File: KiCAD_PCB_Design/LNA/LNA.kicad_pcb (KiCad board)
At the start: 2 copper layers, 47 x 33 mm, 12 parts, among them P1 SMA, P2 3V_SUPPLY, P3 SMA, U1 MGA-62563

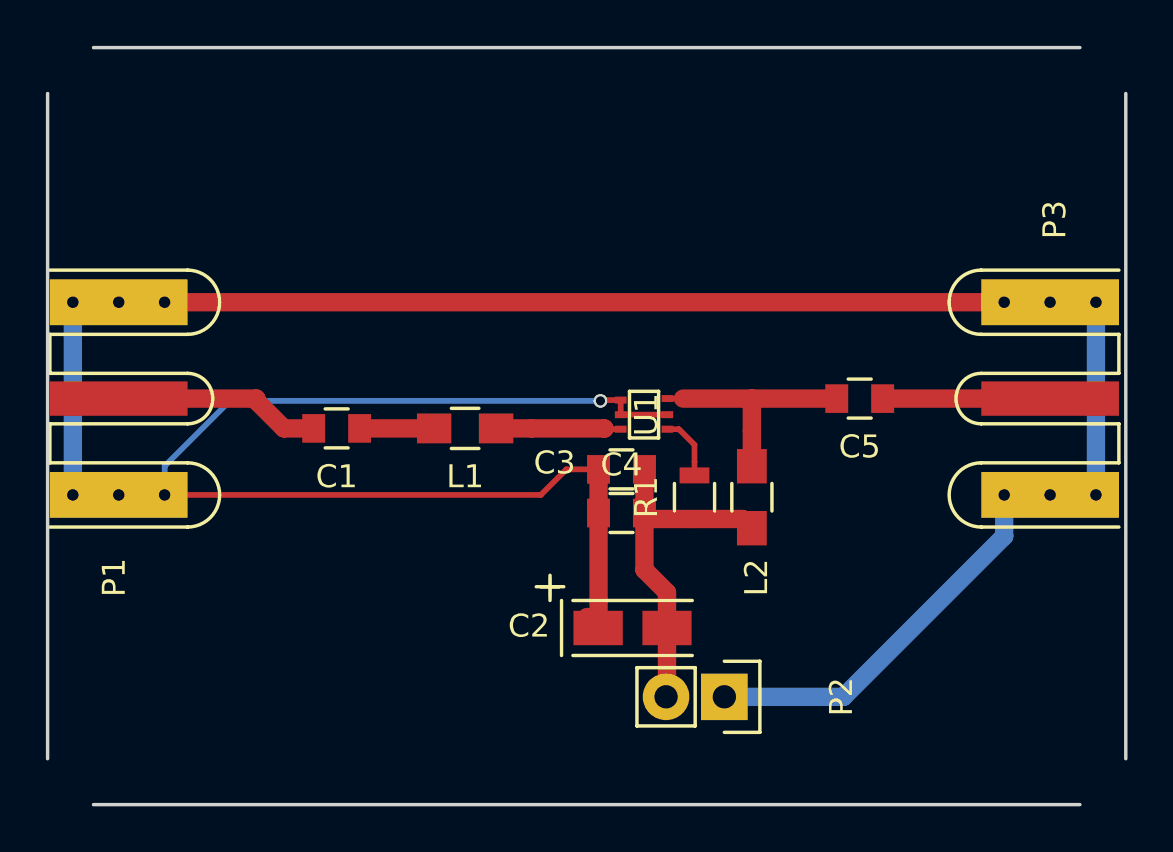
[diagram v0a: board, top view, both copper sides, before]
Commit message: All components made except antenna, Now verifying ..
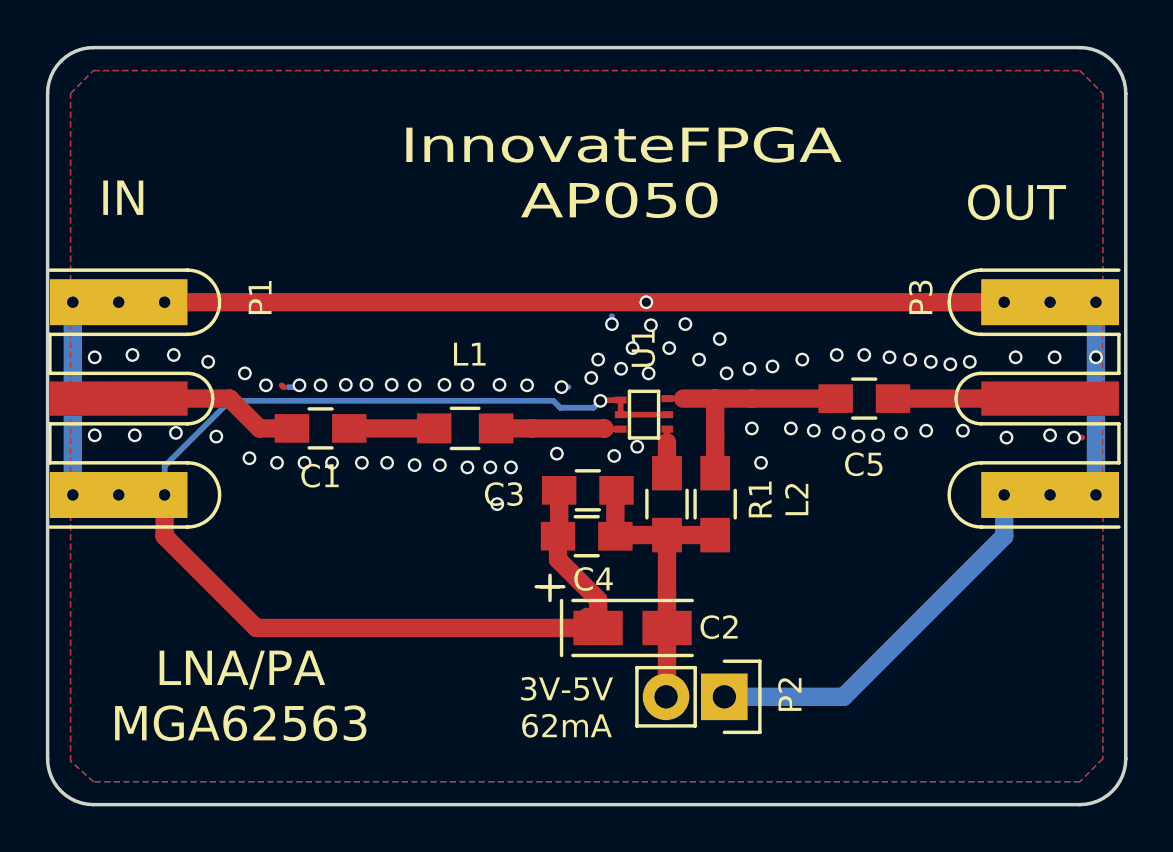
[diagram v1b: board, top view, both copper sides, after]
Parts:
- C1, C3, C4, C5: footprint Capacitors_SMD:C_0805 -> Capacitors_SMD:C_0805_HandSoldering
- L1, L2: footprint Custom_Footprints:Inductor_0805 -> Resistors_SMD:R_0805_HandSoldering
- R1: footprint Resistors_SMD:R_0805 -> Resistors_SMD:R_0805_HandSoldering
- moved C4 1.82 mm to (158.5, 103.3)
- moved C3 1.73 mm to (158.6, 101.3)
- moved L2 1.63 mm to (164.1, 101.9)
- moved R1 1.24 mm to (162.0, 101.9)
- moved C1 0.70 mm to (146.9, 98.6)
- moved C5 0.20 mm to (170.6, 97.3)
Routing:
- net (no net): track 0.00 -> 3.44 mm, vias 0 -> 73
- net GND: track 138.3 -> 141.4 mm, vias 2 -> 4
- net Net-(C2-Pad2): track 15.8 -> 13.5 mm
- net Net-(C1-Pad2): track 9.10 -> 7.74 mm
- net Net-(R1-Pad2): track 2.80 -> 1.92 mm
- added copper zone on B.Cu, net GND
- added copper zone on F.Cu, net GND
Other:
- board text added: "3V-5V 62mA"
- board text added: "FYP-2 MNNIT Allahabad Team 40 Batch 2k18"
- board text added: "IN"
- board text added: "InnovateFPGA AP050"
- board text added: "LNA/PA MGA62563"
- board text added: "OUT"
